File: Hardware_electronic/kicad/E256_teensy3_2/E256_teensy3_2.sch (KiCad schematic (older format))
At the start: 2 parts, among them U1 e256_pad_16x16, U2 Teensy3.2

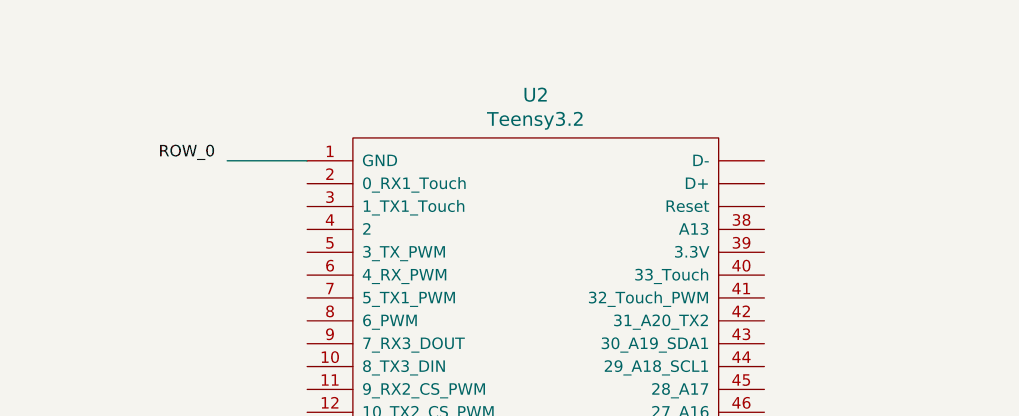
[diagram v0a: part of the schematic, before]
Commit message: Adde pins under PCB to the Teensy lib
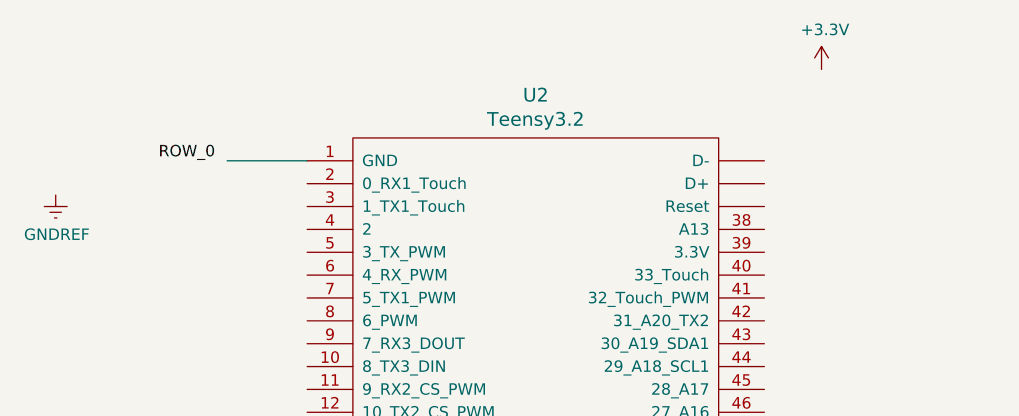
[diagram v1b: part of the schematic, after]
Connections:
- net labels added: +3.3V, GNDREF
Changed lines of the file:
@@
 Text Label 7950 3150 0    50   ~ 0
 ROW_0
+$Comp
+L power:+3.3V #PWR0101
+U 1 1 5DEB6E43
+P 6100 1900
+F 0 "#PWR0101" H 6100 1750 50  0001 C CNN
+F 1 "+3.3V" H 6115 2073 50  0000 C CNN
+F 2 "" H 6100 1900 50  0001 C CNN
+F 3 "" H 6100 1900 50  0001 C CNN
+	1    6100 1900
+	1    0    0    -1
+$EndComp
+$Comp
+L power:GNDREF #PWR0102
+U 1 1 5DEB6EE2
+P 2750 2450
+F 0 "#PWR0102" H 2750 2200 50  0001 C CNN
+F 1 "GNDREF" H 2755 2277 50  0000 C CNN
+F 2 "" H 2750 2450 50  0001 C CNN
+F 3 "" H 2750 2450 50  0001 C CNN
+	1    2750 2450
+	1    0    0    -1
+$EndComp
 $EndSCHEMATC
